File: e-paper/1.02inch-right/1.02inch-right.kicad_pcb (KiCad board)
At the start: 2 copper layers, 40 x 27.6 mm, 25 parts

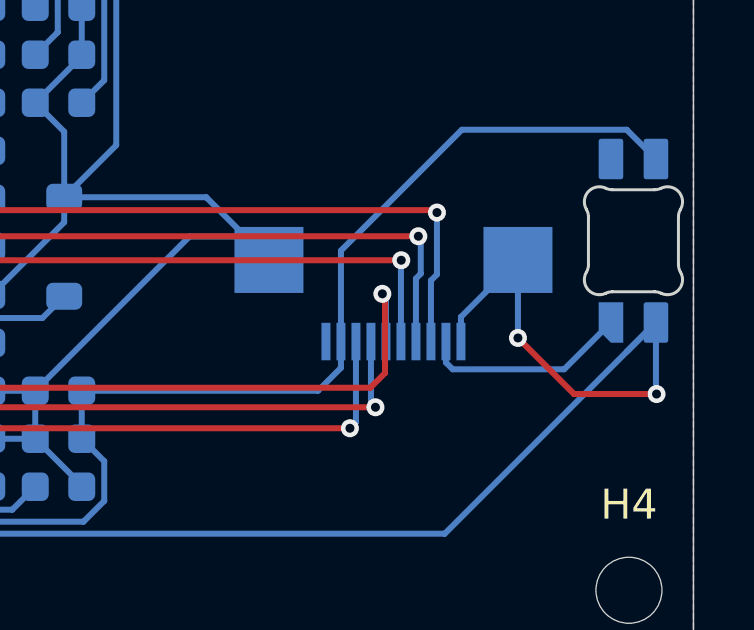
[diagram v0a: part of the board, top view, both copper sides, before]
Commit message: add joystick_fpc_hole
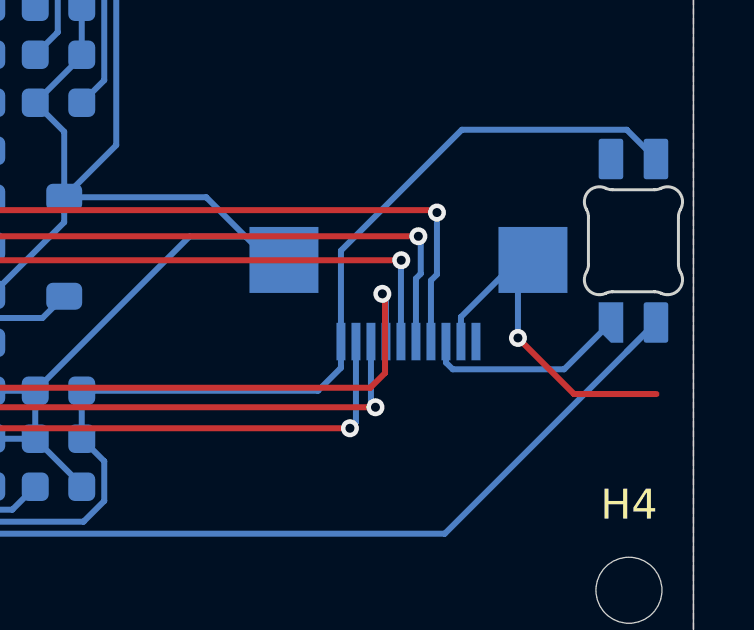
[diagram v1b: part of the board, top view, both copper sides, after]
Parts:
- moved EP_FPC2 0.50 mm to (10.5, 2.00)
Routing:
- net GND: track 151.8 -> 149.4 mm, vias 2 -> 1
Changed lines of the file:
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@@
 	(footprint "ErgoCai.pretty:FPC-SMD_10P-P0.50_JS_AFD01-S10FCA-00"
 		(layer "B.Cu")
-		(at 10 2 180)
+		(at 10.5 2 180)
 		(property "Reference" "EP_FPC2"
 			(at 0 5.36 0)
@@
 	)
 	(via
-		(at 18.77 5.11)
-		(size 0.6)
-		(drill 0.3)
-		(layers "F.Cu" "B.Cu")
-		(net 1)
-	)
-	(via
 		(at 14.15 3.24)
 		(size 0.6)
@@
 	)
 	(segment
-		(start 18.75 5.09)
-		(end 18.77 5.11)
-		(width 0.2)
-		(layer "B.Cu")
-		(net 1)
-	)
-	(segment
 		(start -1.94 6.6)
 		(end -3.38 6.6)
@@
 		(width 0.2)
 		(layer "B.Cu")
-		(net 1)
-	)
-	(segment
-		(start 18.75 2.725)
-		(end 18.75 5.09)
-		(width 0.2)
-		(layer "B.Cu")
